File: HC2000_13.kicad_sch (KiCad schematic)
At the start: 12 parts, among them Q2 8MHz

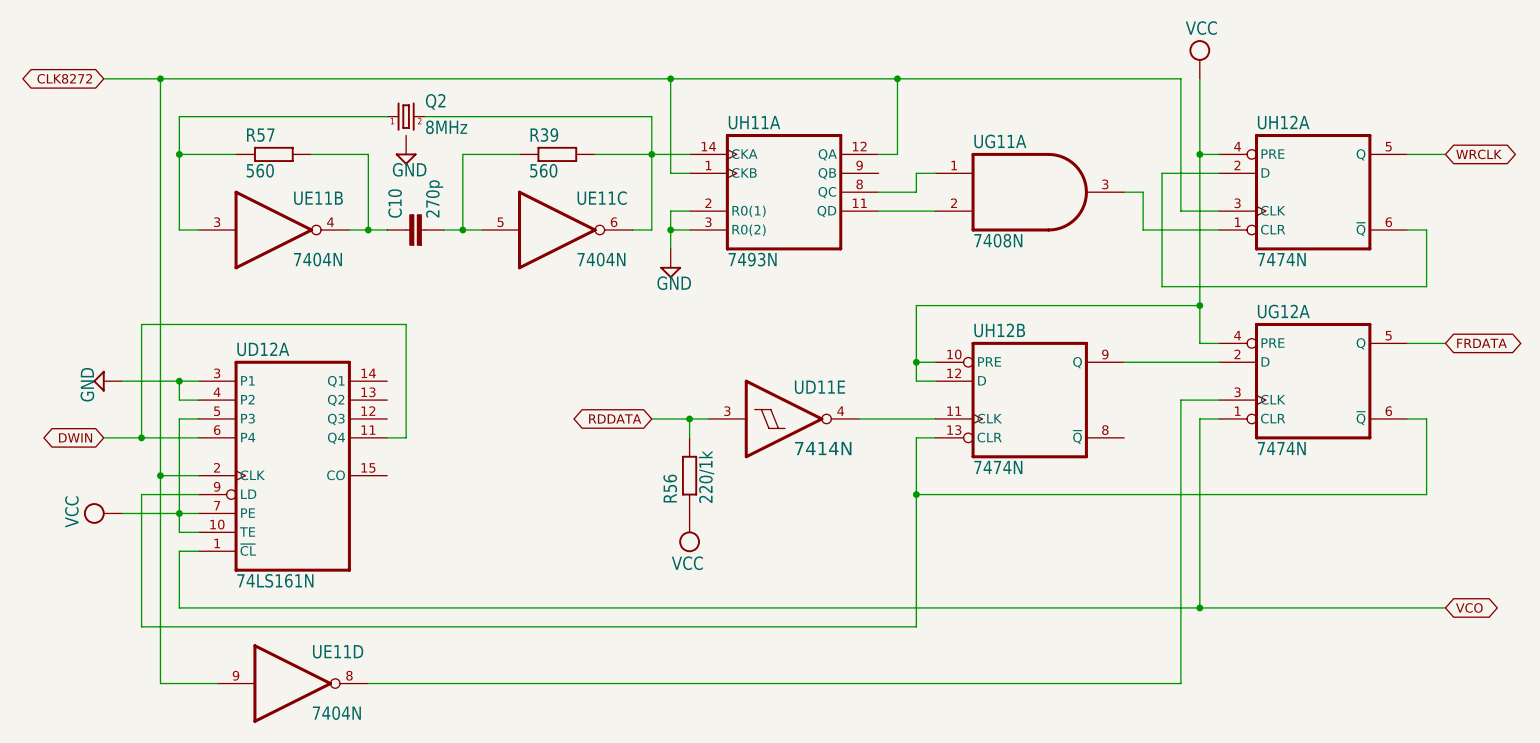
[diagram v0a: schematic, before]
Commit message: Fix errors (IC & unnoticed cut for 1 EPROM)
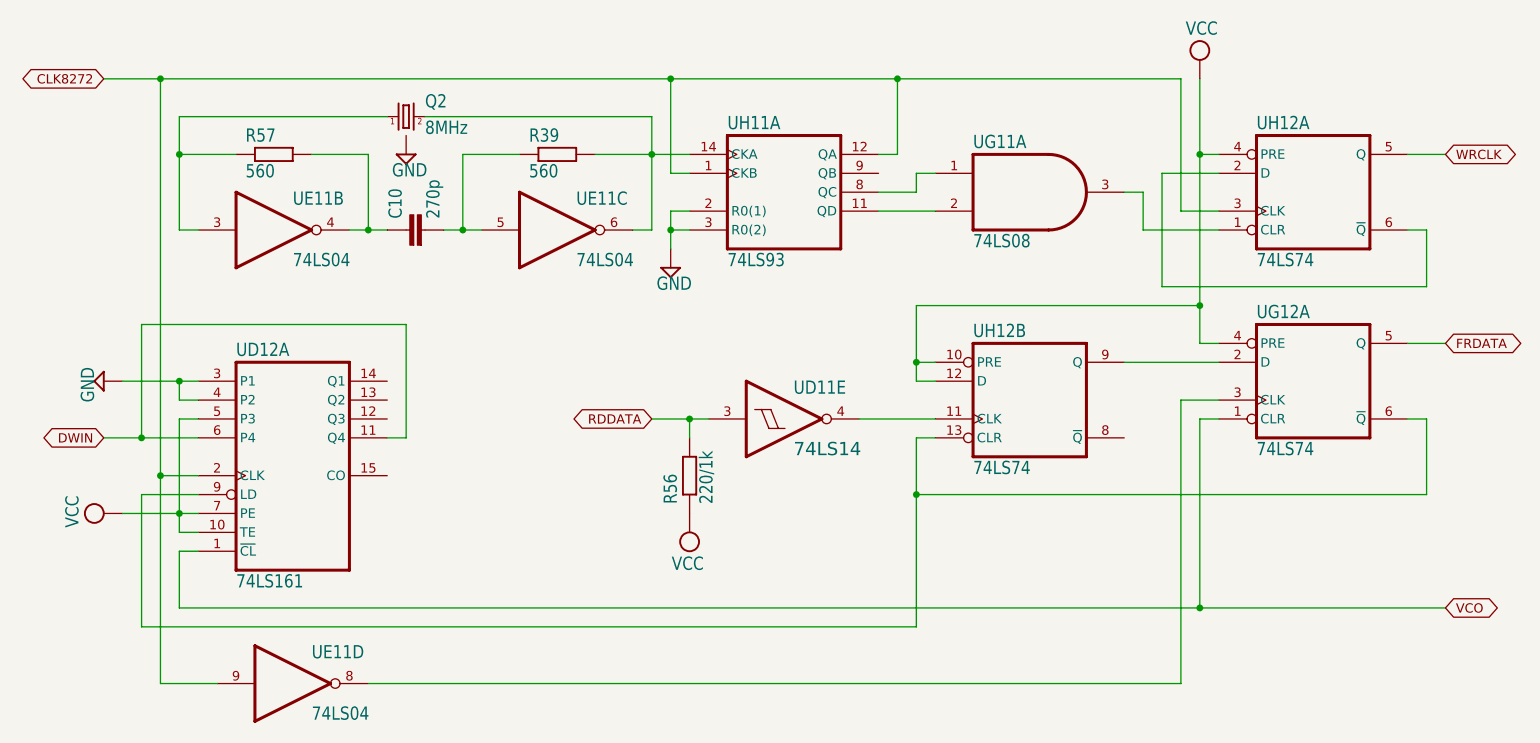
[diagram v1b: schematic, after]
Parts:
- UD11: value 7414N -> 74LS14
- UD12: value 74LS161N -> 74LS161
- UE11: value 7404N -> 74LS04
- UG11: value 7408N -> 74LS08
- UG12, UH12: value 7474N -> 74LS74
- UH11: value 7493N -> 74LS93
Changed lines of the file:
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@@
       (effects (font (size 1.778 1.5113)) (justify left bottom))
     )
-    (property "Value" "7408N" (at 172.72 88.9 0)
+    (property "Value" "74LS08" (at 172.72 88.9 0)
       (effects (font (size 1.778 1.5113)) (justify left bottom))
     )
@@
       (effects (font (size 1.778 1.5113)) (justify left bottom))
     )
-    (property "Value" "7474N" (at 210.82 91.44 0)
+    (property "Value" "74LS74" (at 210.82 91.44 0)
       (effects (font (size 1.778 1.5113)) (justify left bottom))
     )
@@
       (effects (font (size 1.778 1.5113)) (justify left bottom))
     )
-    (property "Value" "7404N" (at 119.38 91.44 0)
+    (property "Value" "74LS04" (at 119.38 91.44 0)
       (effects (font (size 1.778 1.5113)) (justify left bottom))
     )
@@
       (effects (font (size 1.778 1.5113)) (justify left bottom))
     )
-    (property "Value" "7404N" (at 83.82 152.4 0)
+    (property "Value" "74LS04" (at 83.82 152.4 0)
       (effects (font (size 1.778 1.5113)) (justify left bottom))
     )
@@
       (effects (font (size 1.778 1.5113)) (justify left bottom))
     )
-    (property "Value" "7474N" (at 172.72 119.38 0)
+    (property "Value" "74LS74" (at 172.72 119.38 0)
       (effects (font (size 1.778 1.5113)) (justify left bottom))
     )
@@
       (effects (font (size 1.778 1.5113)) (justify left bottom))
     )
-    (property "Value" "7414N" (at 148.59 116.84 0)
+    (property "Value" "74LS14" (at 148.59 116.84 0)
       (effects (font (size 1.778 1.778)) (justify left bottom))
     )
@@
       (effects (font (size 1.778 1.5113)) (justify left bottom))
     )
-    (property "Value" "74LS161N" (at 73.66 134.62 0)
+    (property "Value" "74LS161" (at 73.66 134.62 0)
       (effects (font (size 1.778 1.5113)) (justify left bottom))
     )
@@
       (effects (font (size 1.778 1.5113)) (justify left bottom))
     )
-    (property "Value" "7474N" (at 210.82 116.84 0)
+    (property "Value" "74LS74" (at 210.82 116.84 0)
       (effects (font (size 1.778 1.5113)) (justify left bottom))
     )
@@
       (effects (font (size 1.778 1.5113)) (justify left bottom))
     )
-    (property "Value" "7493N" (at 139.7 91.44 0)
+    (property "Value" "74LS93" (at 139.7 91.44 0)
       (effects (font (size 1.778 1.5113)) (justify left bottom))
     )
@@
       (effects (font (size 1.778 1.5113)) (justify left bottom))
     )
-    (property "Value" "7404N" (at 81.28 91.44 0)
-      (effects (font (size 1.778 1.5113)) (justify left bottom))
-    )
+    (property "Value" "74LS04" (at 81.28 91.44 0)
+      (effects (font (size 1.778 1.5113)) (justify left bottom))
+    )

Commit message: Revision-E
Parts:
- R56: value 220/1k -> 1k
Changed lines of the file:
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@@
       (effects (font (size 1.778 1.5113)) (justify left bottom))
     )
-    (property "Value" "220/1k" (at 137.922 123.19 0)
+    (property "Value" "1k" (at 137.922 123.19 0)
       (effects (font (size 1.778 1.5113)) (justify left bottom))
     )

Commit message: A few minor changes
R62 has value 470 instead of 910 and C6 is missing.
Connected a few conector's shield pins to GND.
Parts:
- C10: footprint HC2000:C025-025X050 -> HC2000:C025-024X044
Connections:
- net at R39.1, UE11.5 (I): now also C10.-; no longer C10.2
- net at R57.2, UE11.4 (O): now also C10.+; no longer C10.1
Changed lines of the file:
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@@
       (effects (font (size 1.778 1.5113)) (justify left bottom))
     )
-    (property "Footprint" "HC2000:C025-025X050" (at 96.52 86.36 0)
+    (property "Footprint" "HC2000:C025-024X044" (at 96.52 86.36 0)
       (effects (font (size 1.27 1.27)) hide)
     )
@@
       (effects (font (size 1.27 1.27)) hide)
     )
-    (pin "1")
-    (pin "2")
+    (pin "+")
+    (pin "-")
     (instances
       (project "HC2000"
